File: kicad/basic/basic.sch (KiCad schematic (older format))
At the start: 18 parts, among them P2 CONN_01X15, P3 CONN_01X15, P4 CONN_01X06, P5 CONN_01X01, P6 CONN_01X01, P7 CONN_01X01, P8 CONN_01X01, P9 CONN_01X06, SW1 SW_PUSH, SW2 SW_PUSH

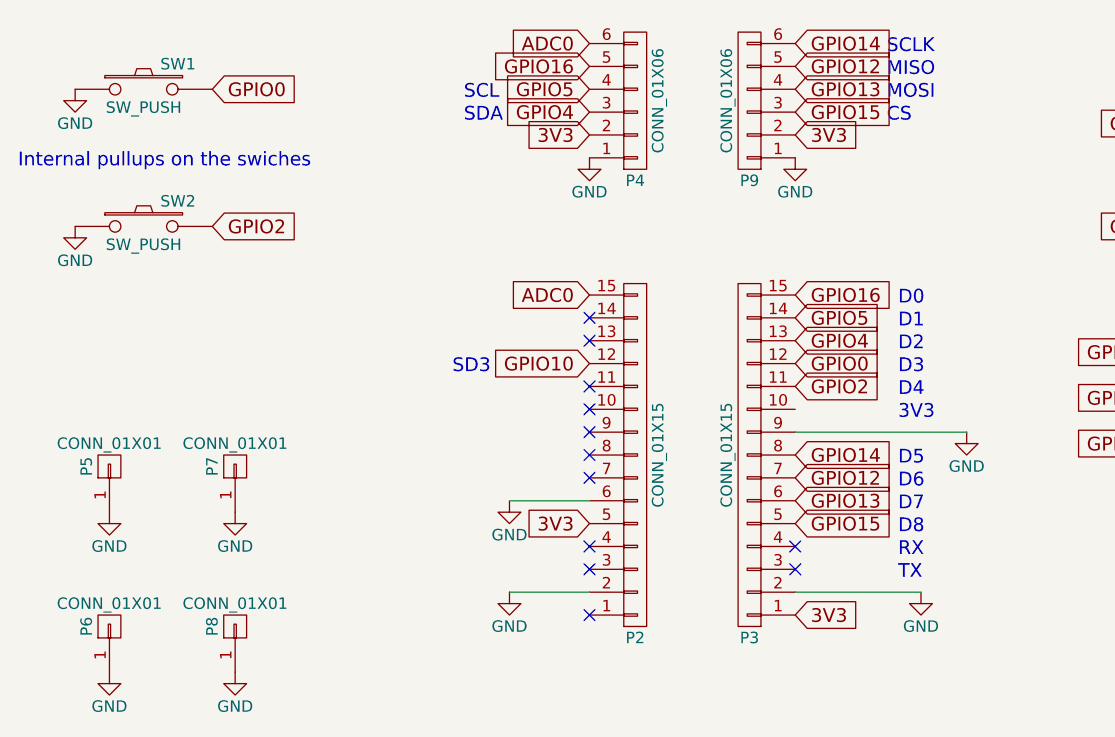
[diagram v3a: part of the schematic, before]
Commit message: Connect the right switch to the header
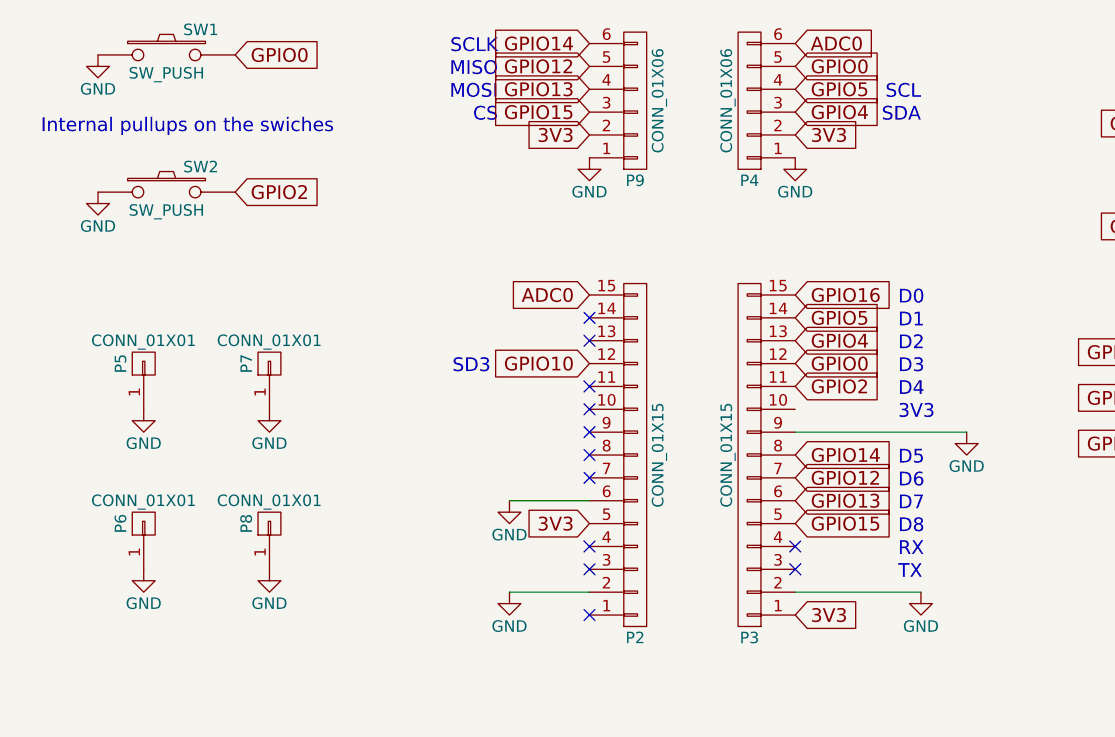
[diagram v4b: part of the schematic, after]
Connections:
- net GPIO0: now also P4.5 (P5)
- net GPIO16: no longer P4.5 (P5)
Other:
- moved on the sheet: P4, P5, P6, P7, P8, P9, SW1, SW2
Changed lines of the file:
@@
 L CONN_01X01 P5
 U 1 1 570F7699
-P 3400 4250
-F 0 "P5" H 3400 4350 50  0000 C CNN
-F 1 "CONN_01X01" V 3500 4250 50  0000 C CNN
-F 2 "Mounting_Holes:MountingHole_3.2mm_M3_ISO14580_Pad" H 3400 4250 50  0001 C CNN
-F 3 "" H 3400 4250 50  0000 C CNN
-	1    3400 4250
+P 3550 3800
+F 0 "P5" H 3550 3900 50  0000 C CNN
+F 1 "CONN_01X01" V 3650 3800 50  0000 C CNN
+F 2 "Mounting_Holes:MountingHole_3.2mm_M3_ISO14580_Pad" H 3550 3800 50  0001 C CNN
+F 3 "" H 3550 3800 50  0000 C CNN
+	1    3550 3800
 	0    -1   -1   0
 $EndComp
@@
 L GND #PWR02
 U 1 1 570F7753
-P 3400 4450
-F 0 "#PWR02" H 3400 4200 50  0001 C CNN
-F 1 "GND" H 3400 4300 50  0000 C CNN
-F 2 "" H 3400 4450 50  0000 C CNN
-F 3 "" H 3400 4450 50  0000 C CNN
-	1    3400 4450
+P 3550 4000
+F 0 "#PWR02" H 3550 3750 50  0001 C CNN
+F 1 "GND" H 3550 3850 50  0000 C CNN
+F 2 "" H 3550 4000 50  0000 C CNN
+F 3 "" H 3550 4000 50  0000 C CNN
+	1    3550 4000
 	1    0    0    -1
 $EndComp
@@
 L CONN_01X01 P7
 U 1 1 570F783F
-P 3950 4250
-F 0 "P7" H 3950 4350 50  0000 C CNN
-F 1 "CONN_01X01" V 4050 4250 50  0000 C CNN
-F 2 "Mounting_Holes:MountingHole_3.2mm_M3_ISO14580_Pad" H 3950 4250 50  0001 C CNN
-F 3 "" H 3950 4250 50  0000 C CNN
-	1    3950 4250
+P 4100 3800
+F 0 "P7" H 4100 3900 50  0000 C CNN
+F 1 "CONN_01X01" V 4200 3800 50  0000 C CNN
+F 2 "Mounting_Holes:MountingHole_3.2mm_M3_ISO14580_Pad" H 4100 3800 50  0001 C CNN
+F 3 "" H 4100 3800 50  0000 C CNN
+	1    4100 3800
 	0    -1   -1   0
 $EndComp
@@
 L GND #PWR03
 U 1 1 570F7845
-P 3950 4450
-F 0 "#PWR03" H 3950 4200 50  0001 C CNN
-F 1 "GND" H 3950 4300 50  0000 C CNN
-F 2 "" H 3950 4450 50  0000 C CNN
-F 3 "" H 3950 4450 50  0000 C CNN
-	1    3950 4450
+P 4100 4000
+F 0 "#PWR03" H 4100 3750 50  0001 C CNN
+F 1 "GND" H 4100 3850 50  0000 C CNN
+F 2 "" H 4100 4000 50  0000 C CNN
+F 3 "" H 4100 4000 50  0000 C CNN
+	1    4100 4000
 	1    0    0    -1
 $EndComp
@@
 L CONN_01X01 P6
 U 1 1 570F78B5
-P 3400 4950
-F 0 "P6" H 3400 5050 50  0000 C CNN
-F 1 "CONN_01X01" V 3500 4950 50  0000 C CNN
-F 2 "Mounting_Holes:MountingHole_3.2mm_M3_ISO14580_Pad" H 3400 4950 50  0001 C CNN
-F 3 "" H 3400 4950 50  0000 C CNN
-	1    3400 4950
+P 3550 4500
+F 0 "P6" H 3550 4600 50  0000 C CNN
+F 1 "CONN_01X01" V 3650 4500 50  0000 C CNN
+F 2 "Mounting_Holes:MountingHole_3.2mm_M3_ISO14580_Pad" H 3550 4500 50  0001 C CNN
+F 3 "" H 3550 4500 50  0000 C CNN
+	1    3550 4500
 	0    -1   -1   0
 $EndComp
@@
 L GND #PWR04
 U 1 1 570F78BB
-P 3400 5150
-F 0 "#PWR04" H 3400 4900 50  0001 C CNN
-F 1 "GND" H 3400 5000 50  0000 C CNN
-F 2 "" H 3400 5150 50  0000 C CNN
-F 3 "" H 3400 5150 50  0000 C CNN
-	1    3400 5150
+P 3550 4700
+F 0 "#PWR04" H 3550 4450 50  0001 C CNN
+F 1 "GND" H 3550 4550 50  0000 C CNN
+F 2 "" H 3550 4700 50  0000 C CNN
+F 3 "" H 3550 4700 50  0000 C CNN
+	1    3550 4700
 	1    0    0    -1
 $EndComp
@@
 L CONN_01X01 P8
 U 1 1 570F78C1
-P 3950 4950
-F 0 "P8" H 3950 5050 50  0000 C CNN
-F 1 "CONN_01X01" V 4050 4950 50  0000 C CNN
-F 2 "Mounting_Holes:MountingHole_3.2mm_M3_ISO14580_Pad" H 3950 4950 50  0001 C CNN
-F 3 "" H 3950 4950 50  0000 C CNN
-	1    3950 4950
+P 4100 4500
+F 0 "P8" H 4100 4600 50  0000 C CNN
+F 1 "CONN_01X01" V 4200 4500 50  0000 C CNN
+F 2 "Mounting_Holes:MountingHole_3.2mm_M3_ISO14580_Pad" H 4100 4500 50  0001 C CNN
+F 3 "" H 4100 4500 50  0000 C CNN
+	1    4100 4500
 	0    -1   -1   0
 $EndComp
@@
 L GND #PWR05
 U 1 1 570F78C7
-P 3950 5150
-F 0 "#PWR05" H 3950 4900 50  0001 C CNN
-F 1 "GND" H 3950 5000 50  0000 C CNN
-F 2 "" H 3950 5150 50  0000 C CNN
-F 3 "" H 3950 5150 50  0000 C CNN
-	1    3950 5150
+P 4100 4700
+F 0 "#PWR05" H 4100 4450 50  0001 C CNN
+F 1 "GND" H 4100 4550 50  0000 C CNN
+F 2 "" H 4100 4700 50  0000 C CNN
+F 3 "" H 4100 4700 50  0000 C CNN
+	1    4100 4700
 	1    0    0    -1
 $EndComp
@@
 L SW_PUSH SW1
 U 1 1 570F9210
-P 3550 2600
-F 0 "SW1" H 3700 2710 50  0000 C CNN
-F 1 "SW_PUSH" H 3550 2520 50  0000 C CNN
-F 2 "Buttons_Switches_ThroughHole:SW_PUSH_SMALL" H 3550 2600 50  0001 C CNN
-F 3 "" H 3550 2600 50  0000 C CNN
-	1    3550 2600
+P 3650 2450
+F 0 "SW1" H 3800 2560 50  0000 C CNN
+F 1 "SW_PUSH" H 3650 2370 50  0000 C CNN
+F 2 "Buttons_Switches_ThroughHole:SW_PUSH_SMALL" H 3650 2450 50  0001 C CNN
+F 3 "" H 3650 2450 50  0000 C CNN
+	1    3650 2450
 	1    0    0    -1
 $EndComp
@@
 L SW_PUSH SW2
 U 1 1 570F927F
-P 3550 3200
-F 0 "SW2" H 3700 3310 50  0000 C CNN
-F 1 "SW_PUSH" H 3550 3120 50  0000 C CNN
-F 2 "Buttons_Switches_ThroughHole:SW_PUSH_SMALL" H 3550 3200 50  0001 C CNN
-F 3 "" H 3550 3200 50  0000 C CNN
-	1    3550 3200
+P 3650 3050
+F 0 "SW2" H 3800 3160 50  0000 C CNN
+F 1 "SW_PUSH" H 3650 2970 50  0000 C CNN
+F 2 "Buttons_Switches_ThroughHole:SW_PUSH_SMALL" H 3650 3050 50  0001 C CNN
+F 3 "" H 3650 3050 50  0000 C CNN
+	1    3650 3050
 	1    0    0    -1
 $EndComp
@@
 Text GLabel 5500 3500 0    60   Input ~ 0
 ADC0
-Text GLabel 5500 2400 0    60   Input ~ 0
+Text GLabel 6400 2400 2    60   Input ~ 0
 ADC0
 Text GLabel 6400 4500 2    60   Input ~ 0
@@
 L GND #PWR012
 U 1 1 570FB498
-P 3250 2600
-F 0 "#PWR012" H 3250 2350 50  0001 C CNN
-F 1 "GND" H 3250 2450 50  0000 C CNN
-F 2 "" H 3250 2600 50  0000 C CNN
-F 3 "" H 3250 2600 50  0000 C CNN
-	1    3250 2600
+P 3350 2450
+F 0 "#PWR012" H 3350 2200 50  0001 C CNN
+F 1 "GND" H 3350 2300 50  0000 C CNN
+F 2 "" H 3350 2450 50  0000 C CNN
+F 3 "" H 3350 2450 50  0000 C CNN
+	1    3350 2450
 	1    0    0    -1
 $EndComp
@@
 L GND #PWR013
 U 1 1 570FB53B
-P 3250 3200
-F 0 "#PWR013" H 3250 2950 50  0001 C CNN
-F 1 "GND" H 3250 3050 50  0000 C CNN
-F 2 "" H 3250 3200 50  0000 C CNN
-F 3 "" H 3250 3200 50  0000 C CNN
-	1    3250 3200
+P 3350 3050
+F 0 "#PWR013" H 3350 2800 50  0001 C CNN
+F 1 "GND" H 3350 2900 50  0000 C CNN
+F 2 "" H 3350 3050 50  0000 C CNN
+F 3 "" H 3350 3050 50  0000 C CNN
+	1    3350 3050
 	1    0    0    -1
 $EndComp
@@
 L CONN_01X06 P4
 U 1 1 570FA03F
+P 6200 2650
+F 0 "P4" H 6200 3000 50  0000 C CNN
+F 1 "CONN_01X06" V 6300 2650 50  0000 C CNN
+F 2 "Socket_Strips:Socket_Strip_Straight_1x06" H 6200 2650 50  0001 C CNN
+F 3 "" H 6200 2650 50  0000 C CNN
+	1    6200 2650
+	-1   0    0    1
+$EndComp
+$Comp
+L CONN_01X06 P9
+U 1 1 570FA0CA
 P 5700 2650
-F 0 "P4" H 5700 3000 50  0000 C CNN
+F 0 "P9" H 5700 3000 50  0000 C CNN
 F 1 "CONN_01X06" V 5800 2650 50  0000 C CNN
 F 2 "Socket_Strips:Socket_Strip_Straight_1x06" H 5700 2650 50  0001 C CNN
@@
 $EndComp
 $Comp
-L CONN_01X06 P9
-U 1 1 570FA0CA
-P 6200 2650
-F 0 "P9" H 6200 3000 50  0000 C CNN
-F 1 "CONN_01X06" V 6300 2650 50  0000 C CNN
-F 2 "Socket_Strips:Socket_Strip_Straight_1x06" H 6200 2650 50  0001 C CNN
-F 3 "" H 6200 2650 50  0000 C CNN
-	1    6200 2650
-	-1   0    0    1
-$EndComp
-$Comp
 L GND #PWR014
 U 1 1 570FA133
+P 5500 2900
+F 0 "#PWR014" H 5500 2650 50  0001 C CNN
+F 1 "GND" H 5500 2750 50  0000 C CNN
+F 2 "" H 5500 2900 50  0000 C CNN
+F 3 "" H 5500 2900 50  0000 C CNN
+	1    5500 2900
+	-1   0    0    -1
+$EndComp
+$Comp
+L GND #PWR015
+U 1 1 570FA17D
 P 6400 2900
-F 0 "#PWR014" H 6400 2650 50  0001 C CNN
+F 0 "#PWR015" H 6400 2650 50  0001 C CNN
 F 1 "GND" H 6400 2750 50  0000 C CNN
 F 2 "" H 6400 2900 50  0000 C CNN
 F 3 "" H 6400 2900 50  0000 C CNN
 	1    6400 2900
-	1    0    0    -1
-$EndComp
-$Comp
-L GND #PWR015
-U 1 1 570FA17D
-P 5500 2900
-F 0 "#PWR015" H 5500 2650 50  0001 C CNN
-F 1 "GND" H 5500 2750 50  0000 C CNN
-F 2 "" H 5500 2900 50  0000 C CNN
-F 3 "" H 5500 2900 50  0000 C CNN
-	1    5500 2900
-	1    0    0    -1
-$EndComp
+	-1   0    0    -1
+$EndComp
+Text GLabel 5500 2700 0    60   Input ~ 0
+GPIO15
+Text GLabel 5500 2600 0    60   Input ~ 0
+GPIO13
+Text GLabel 5500 2400 0    60   Input ~ 0
+GPIO14
+Text GLabel 6400 2600 2    60   Input ~ 0
+GPIO5
 Text GLabel 6400 2700 2    60   Input ~ 0
-GPIO15
-Text GLabel 6400 2600 2    60   Input ~ 0
-GPIO13
-Text GLabel 6400 2400 2    60   Input ~ 0
-GPIO14
-Text GLabel 5500 2600 0    60   Input ~ 0
-GPIO5
-Text GLabel 5500 2700 0    60   Input ~ 0
 GPIO4
 Text GLabel 8050 3950 0    60   Input ~ 0
@@
 Text GLabel 8150 2750 0    60   Input ~ 0
 GPIO13
-Text GLabel 3850 2600 2    60   Input ~ 0
+Text GLabel 3950 2450 2    60   Input ~ 0
 GPIO0
-Text GLabel 3850 3200 2    60   Input ~ 0
+Text GLabel 3950 3050 2    60   Input ~ 0
 GPIO2
 $Comp
@@
 Text GLabel 6400 4200 2    60   Input ~ 0
 GPIO14
-Text GLabel 5500 2500 0    60   Input ~ 0
-GPIO16
-Text GLabel 5500 2800 0    60   Input ~ 0
+Text GLabel 6400 2800 2    60   Input ~ 0
 3V3
 Wire Wire Line
@@
 Text Label 8500 3200 0    60   ~ 0
 S_RED
-Text GLabel 6400 2500 2    60   Input ~ 0
+Text GLabel 5500 2500 0    60   Input ~ 0
 GPIO12
 Text GLabel 5500 3800 0    60   Input ~ 0
@@
 Text GLabel 6400 3500 2    60   Input ~ 0
 GPIO16
-Text GLabel 6400 2800 2    60   Input ~ 0
+Text GLabel 5500 2800 0    60   Input ~ 0
 3V3
-Text Notes 6800 2550 0    60   ~ 0
+Text Notes 5100 2550 2    60   ~ 0
 MISO
-Text Notes 6800 2450 0    60   ~ 0
+Text Notes 5100 2450 2    60   ~ 0
 SCLK
-Text Notes 6800 2650 0    60   ~ 0
+Text Notes 5100 2650 2    60   ~ 0
 MOSI
-Text Notes 6800 2750 0    60   ~ 0
+Text Notes 5100 2750 2    60   ~ 0
 CS
-Text Notes 4950 2750 0    60   ~ 0
+Text Notes 6950 2750 2    60   ~ 0
 SDA
-Text Notes 4950 2650 0    60   ~ 0
+Text Notes 6950 2650 2    60   ~ 0
 SCL
 Text GLabel 6400 3700 2    60   Input ~ 0
@@
 Text Notes 4900 3850 0    60   ~ 0
 SD3
-Text Notes 3000 2950 0    60   ~ 0
+Text Notes 3100 2800 0    60   ~ 0
 Internal pullups on the swiches
+Text GLabel 6400 2500 2    60   Input ~ 0
+GPIO0
 $EndSCHEMATC

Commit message: Use gpio16 instead of gpio0
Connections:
- net GPIO0: no longer P4.5 (P5), SW1.2
- net GPIO16: now also P4.5 (P5), SW1.2
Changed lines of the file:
@@
 GPIO13
 Text GLabel 3950 2450 2    60   Input ~ 0
-GPIO0
+GPIO16
 Text GLabel 3950 3050 2    60   Input ~ 0
 GPIO2
@@
 Internal pullups on the swiches
 Text GLabel 6400 2500 2    60   Input ~ 0
-GPIO0
+GPIO16
 $EndSCHEMATC

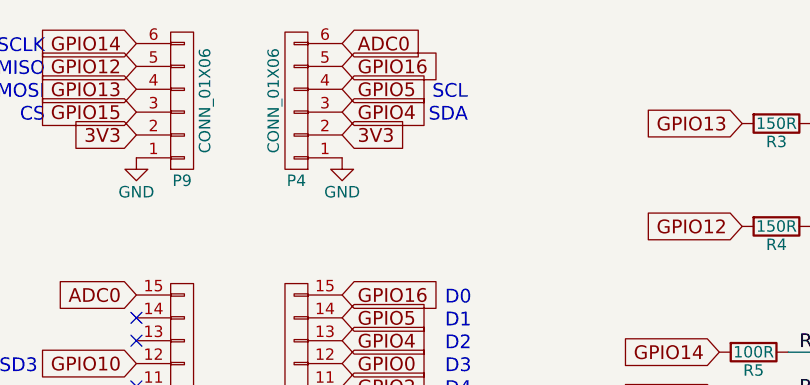
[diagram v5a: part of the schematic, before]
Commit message: Swap SDA & SCL on the header
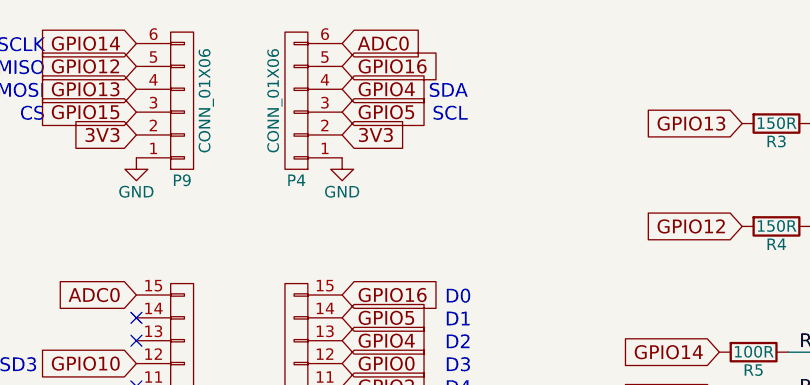
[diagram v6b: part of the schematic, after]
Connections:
- net GPIO4: now also P4.4 (P4); no longer P4.3 (P3)
- net GPIO5: now also P4.3 (P3); no longer P4.4 (P4)
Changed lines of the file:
@@
 Text GLabel 5500 2400 0    60   Input ~ 0
 GPIO14
+Text GLabel 6400 2700 2    60   Input ~ 0
+GPIO5
 Text GLabel 6400 2600 2    60   Input ~ 0
-GPIO5
-Text GLabel 6400 2700 2    60   Input ~ 0
 GPIO4
 Text GLabel 8050 3950 0    60   Input ~ 0
@@
 Text Notes 5100 2750 2    60   ~ 0
 CS
+Text Notes 6950 2650 2    60   ~ 0
+SDA
 Text Notes 6950 2750 2    60   ~ 0
-SDA
-Text Notes 6950 2650 2    60   ~ 0
 SCL
 Text GLabel 6400 3700 2    60   Input ~ 0

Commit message: External power
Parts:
- added P1: EXT_PWR, Pin_Headers:Pin_Header_Straight_1x02, symbol CONN_01X02
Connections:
- net GND: now also P1.1 (P1)
- net VIN: now reaches P2.1 (P1)
- net VIN: now also P1.2 (P2)
- no-connect marks 12 -> 11
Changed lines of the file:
@@
 NoConn ~ 5500 4600
 NoConn ~ 5500 4700
-NoConn ~ 5500 4900
 Wire Wire Line
 	5150 4400 5500 4400
@@
 Text GLabel 6400 2500 2    60   Input ~ 0
 GPIO16
+$Comp
+L CONN_01X02 P1
+U 1 1 57175B5D
+P 2425 3950
+F 0 "P1" H 2425 4100 50  0000 C CNN
+F 1 "EXT_PWR" V 2525 3950 50  0000 C CNN
+F 2 "Pin_Headers:Pin_Header_Straight_1x02" H 2425 3950 50  0001 C CNN
+F 3 "" H 2425 3950 50  0000 C CNN
+	1    2425 3950
+	1    0    0    1
+$EndComp
+$Comp
+L GND #PWR016
+U 1 1 57175D11
+P 2225 4000
+F 0 "#PWR016" H 2225 3750 50  0001 C CNN
+F 1 "GND" H 2225 3850 50  0000 C CNN
+F 2 "" H 2225 4000 50  0000 C CNN
+F 3 "" H 2225 4000 50  0000 C CNN
+	1    2225 4000
+	1    0    0    -1
+$EndComp
+Text GLabel 5500 4900 0    60   Input ~ 0
+VIN
+Text GLabel 2225 3900 0    60   Input ~ 0
+VIN
 $EndSCHEMATC
